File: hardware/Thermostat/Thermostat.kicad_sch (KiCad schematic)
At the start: 46 parts, among them J1 Barrel_Jack_Switch, J2 Conn_01x02_Pin, J3 AVR-ISP-6, J4 MainConnectorr, K1 G6E, K2 G6E, K3 G6E, K4 G6E, SW1 12MM, SW2 12MM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

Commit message: Battery?
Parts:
- added BT1: Battery_Cell, Battery:BatteryHolder_LINX_BAT-HLD-012-SMT, symbol Device:Battery_Cell
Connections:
- net GND: now also BT1.2 (-); no longer U8.3 (VBAT)
- new net: BT1.1 (+), U8.3 (VBAT)
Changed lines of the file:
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@@
+	)
+	(symbol
+		(lib_id "Device:Battery_Cell")
+		(at 182.88 137.16 90)
+		(unit 1)
+		(exclude_from_sim no)
+		(in_bom yes)
+		(on_board yes)
+		(dnp no)
+		(property "Reference" "BT1"
+			(at 193.802 136.652 90)
+			(effects
+				(font
+					(size 1.27 1.27)
+				)
+			)
+		)
+		(property "Value" "Battery_Cell"
+			(at 188.214 134.62 90)
+			(effects
+				(font
+					(size 1.27 1.27)
+				)
+			)
+		)
+		(property "Footprint" "Battery:BatteryHolder_LINX_BAT-HLD-012-SMT"
+			(at 181.356 137.16 90)
+			(effects
+				(font
+					(size 1.27 1.27)
+				)
+				(hide yes)
+			)
+		)
+		(property "Datasheet" "~"
+			(at 181.356 137.16 90)
+			(effects
+				(font
+					(size 1.27 1.27)
+				)
+				(hide yes)
+			)
+		)
+		(property "Description" "Single-cell battery"
+			(at 182.88 137.16 0)
+			(effects
+				(font
+					(size 1.27 1.27)
+				)
+				(hide yes)
+			)
+		)
+		(property "Sim.Device" "V"
+			(at 182.88 137.16 0)
+			(effects
+				(font
+					(size 1.27 1.27)
+				)
+				(hide yes)
+			)
+		)
+		(property "Sim.Type" "DC"
+			(at 182.88 137.16 0)
+			(effects
+				(font
+					(size 1.27 1.27)
+				)
+				(hide yes)
+			)
+		)
+		(property "Sim.Pins" "1=+ 2=-"
+			(at 182.88 137.16 0)
+			(effects
+				(font
+					(size 1.27 1.27)
+				)
+				(hide yes)
+			)
+		)
+		(pin "2"
+		)
+		(pin "1"
+		)
+		(instances
+			(project ""
+				(path "/dae3c193-ffe6-4911-a810-cfe956c95f3b"
+					(reference "BT1")
+					(unit 1)
+				)
+			)
+		)
 	)
 	(symbol
@@
 	(symbol
 		(lib_id "power:GND")
-		(at 177.8 137.16 90)
+		(at 185.42 137.16 90)
 		(unit 1)
 		(exclude_from_sim no)
@@
 		(dnp no)
 		(property "Reference" "#PWR030"
-			(at 184.15 137.16 0)
+			(at 191.77 137.16 0)
 			(effects
 				(font
@@
 		)
 		(property "Value" "GND"
-			(at 182.372 137.16 90)
+			(at 189.992 137.16 90)
 			(effects
 				(font
@@
 		)
 		(property "Footprint" ""
-			(at 177.8 137.16 0)
+			(at 185.42 137.16 0)
 			(effects
 				(font
@@
 		)
 		(property "Datasheet" ""
-			(at 177.8 137.16 0)
+			(at 185.42 137.16 0)
 			(effects
 				(font
@@
 		)
 		(property "Description" "Power symbol creates a global label with name \"GND\" , ground"
-			(at 177.8 137.16 0)
-			(effects
-				(font
+			(at 185.42 137.16 0)
+			(effects
+				(font

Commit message: Get in battery
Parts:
- BT1: footprint Battery:BatteryHolder_LINX_BAT-HLD-012-SMT -> Battery:BatteryHolder_Keystone_3000_1x12mm
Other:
- moved on the sheet: BT1, C10, C7, C8, C9, R6, R7, U1, U2, U8, U9, Y3

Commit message: Fixes from Cyber City Circuits review
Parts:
- removed D5: 1N4007, Diode_THT:D_DO-41_SOD81_P10.16mm_Horizontal, symbol Diode:1N4007
- added D1: SS33, Diode_SMD:D_SMA, symbol Diode:SS33
- added R2: 4.7k, Resistor_SMD:R_0603_1608Metric, symbol Device:R_US
- R1: value 5k -> 10k
- R6, R7: value 5k -> 4.7k
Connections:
- net +5V: now also U5.18 (AVCC), U5.20 (AREF), R2.1; no longer U1.6 (^RESET)
- net 24VDC: now also D1.1 (K)
- net GND: no longer U5.18 (AVCC), U5.20 (AREF)
- net at J1.1: now also D1.2 (A)
- net ^SCRESET: now reaches U5.12 (PB0)
- net ^SCRESET: now also U1.6 (^RESET), R2.2
- no-connect marks 16 -> 15

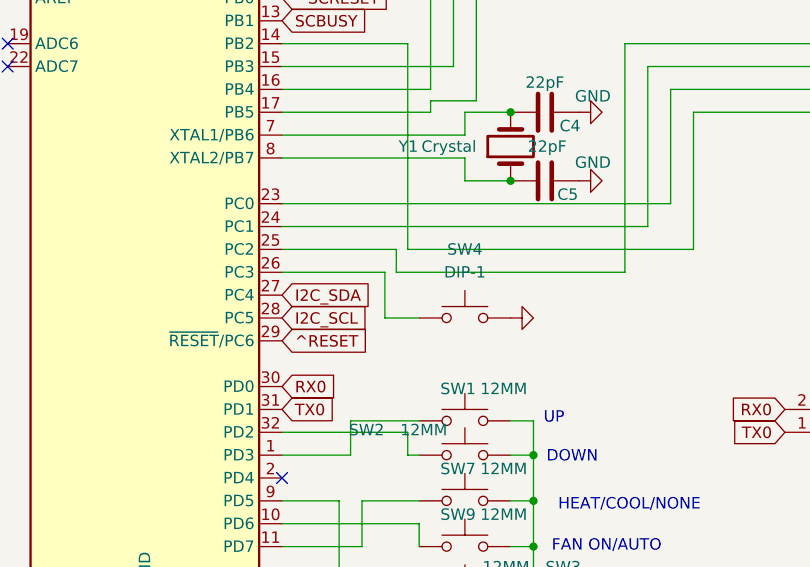
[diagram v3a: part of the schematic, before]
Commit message: Remove physical Reverse Valve button and put it in save state instead
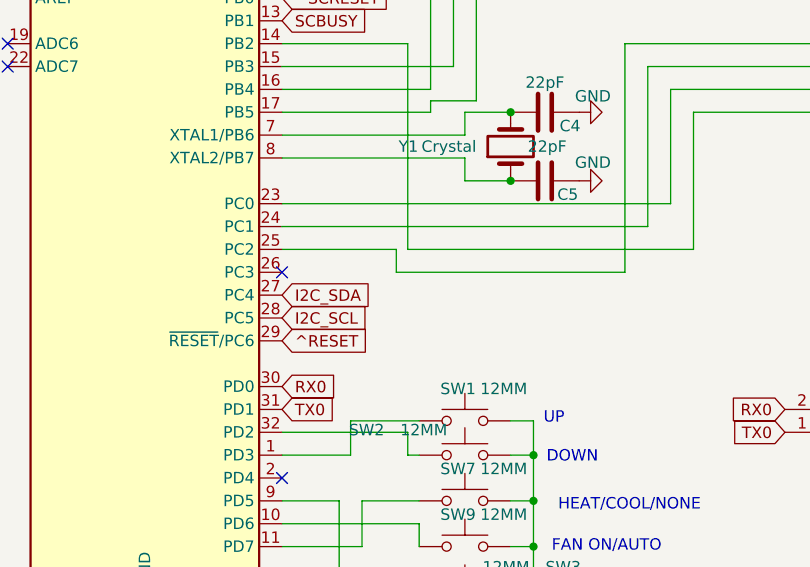
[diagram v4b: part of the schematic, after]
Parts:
- removed SW4: DIP-1, Button_Switch_SMD:SW_DIP_SPSTx01_Slide_6.7x4.1mm_W6.73mm_P2.54mm_LowProfile_JPin, symbol Switch:SW_Push
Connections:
- no-connect marks 15 -> 16
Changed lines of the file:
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@@
 	)
 	(no_connect
+		(at 50.8 140.97)
+	)
+	(no_connect
 		(at 113.03 87.63)
 	)
@@
 	(wire
 		(pts
-			(xy 62.23 140.97) (xy 62.23 146.05)
-		)
-		(stroke
-			(width 0)
-			(type default)
-		)
-	)
-	(wire
-		(pts
 			(xy 137.16 39.37) (xy 137.16 40.64)
 		)
@@
 	(wire
 		(pts
-			(xy 62.23 146.05) (xy 66.04 146.05)
-		)
-		(stroke
-			(width 0)
-			(type default)
-		)
-	)
-	(wire
-		(pts
 			(xy 119.38 110.49) (xy 121.92 110.49)
 		)
@@
 	(wire
 		(pts
-			(xy 50.8 140.97) (xy 62.23 140.97)
-		)
-		(stroke
-			(width 0)
-			(type default)
-		)
-	)
-	(wire
-		(pts
 			(xy 152.4 38.1) (xy 152.4 40.64)
 		)
@@
 	)
 	(symbol
-		(lib_id "Switch:SW_Push")
-		(at 71.12 146.05 0)
-		(unit 1)
-		(exclude_from_sim no)
-		(in_bom yes)
-		(on_board yes)
-		(dnp no)
-		(fields_autoplaced yes)
-		(property "Reference" "SW4"
-			(at 71.12 138.43 0)
-			(effects
-				(font
-					(size 1.27 1.27)
-				)
-			)
-		)
-		(property "Value" "DIP-1"
-			(at 71.12 140.97 0)
-			(effects
-				(font
-					(size 1.27 1.27)
-				)
-			)
-		)
-		(property "Footprint" "Button_Switch_SMD:SW_DIP_SPSTx01_Slide_6.7x4.1mm_W6.73mm_P2.54mm_LowProfile_JPin"
-			(at 71.12 140.97 0)
-			(effects
-				(font
-					(size 1.27 1.27)
-				)
-				(hide yes)
-			)
-		)
-		(property "Datasheet" "~"
-			(at 71.12 140.97 0)
-			(effects
-				(font
-					(size 1.27 1.27)
-				)
-				(hide yes)
-			)
-		)
-		(property "Description" "Push button switch, generic, two pins"
-			(at 71.12 146.05 0)
-			(effects
-				(font
-					(size 1.27 1.27)
-				)
-				(hide yes)
-			)
-		)
-		(pin "2"
-		)
-		(pin "1"
-		)
-		(instances
-			(project "Thermostat"
-				(path "/dae3c193-ffe6-4911-a810-cfe956c95f3b"
-					(reference "SW4")
-					(unit 1)
-				)
-			)
-		)
-	)
-	(symbol
 		(lib_id "power:+5V")
 		(at 207.01 123.19 0)
@@
 					(unit 1)
 				)
-			)
-		)
-	)
-	(symbol
-		(lib_id "power:GND")
-		(at 76.2 146.05 90)
-		(unit 1)
-		(exclude_from_sim no)
-		(in_bom yes)
-		(on_board yes)
-		(dnp no)
-		(property "Reference" "#PWR06"
-			(at 82.55 146.05 0)
-			(effects
-				(font
-					(size 1.27 1.27)
-				)
-				(hide yes)
-			)
-		)
-		(property "Value" "GND"
-			(at 83.058 147.828 90)
-			(effects
-				(font
-					(size 1.27 1.27)
-				)
-				(hide yes)
-			)
-		)
-		(property "Footprint" ""
-			(at 76.2 146.05 0)
-			(effects
-				(font
-					(size 1.27 1.27)
-				)
-				(hide yes)
-			)
-		)
-		(property "Datasheet" ""
-			(at 76.2 146.05 0)
-			(effects
-				(font
-					(size 1.27 1.27)
-				)
-				(hide yes)
-			)
-		)
-		(property "Description" "Power symbol creates a global label with name \"GND\" , ground"
-			(at 76.2 146.05 0)
-			(effects
-				(font
-					(size 1.27 1.27)
-				)
-				(hide yes)
-			)
-		)
-		(pin "1"
-		)
-		(instances
-			(project "Thermostat"
-				(path "/dae3c193-ffe6-4911-a810-cfe956c95f3b"
-					(reference "#PWR06")
-					(unit 1)
-				)

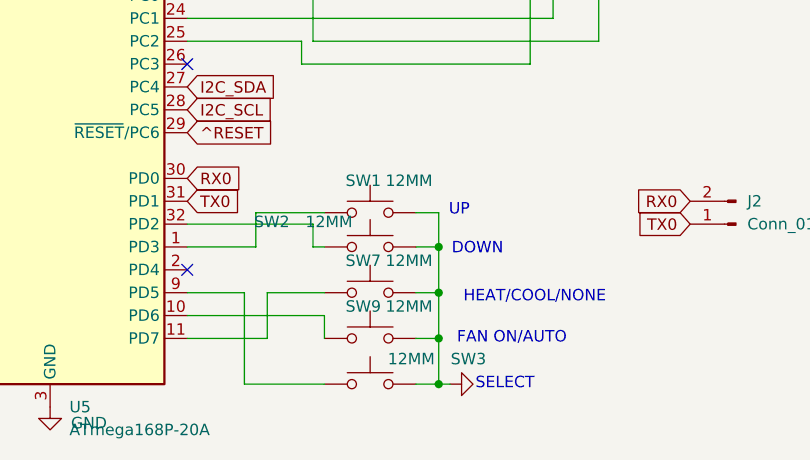
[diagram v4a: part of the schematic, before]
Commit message: Put switches in order and move resistor
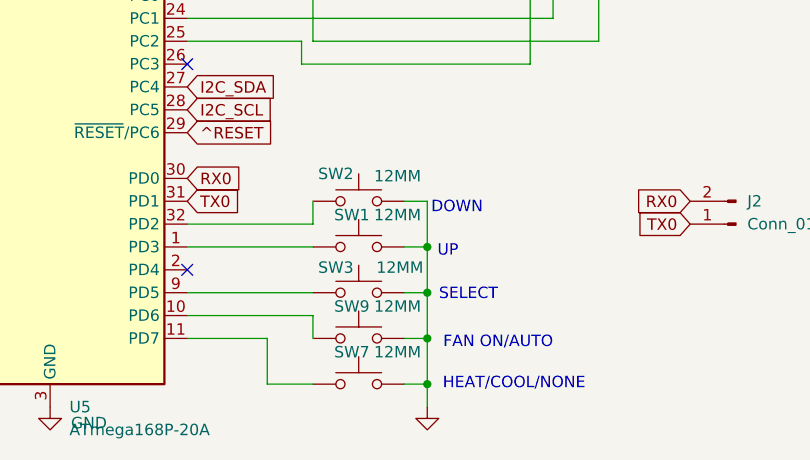
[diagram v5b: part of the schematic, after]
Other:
- moved on the sheet: SW1, SW2, SW3, SW7, SW9

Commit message: Hardware work
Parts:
- removed J1: Barrel_Jack_Switch, Connector_BarrelJack:BarrelJack_Wuerth_6941xx301002, symbol Connector:Barrel_Jack_Switch
- added J5: Screw_Terminal_01x02, TerminalBlock_MetzConnect:TerminalBlock_MetzConnect_Type094_RT03502HBLU_1x02_P5.00mm_Horizontal, symbol Connector:Screw_Terminal_01x02
- BT1: footprint Battery:BatteryHolder_Keystone_3000_1x12mm -> ThermostatFootprints:BS-12-B3AA011
- C1, C2, C3: footprint Capacitor_SMD:C_1808_4520Metric -> Capacitor_SMD:C_1210_3225Metric
- U3: value ~ -> (none)
- Y3: footprint Crystal:Crystal_SMD_5032-2Pin_5.0x3.2mm -> Crystal:Crystal_SMD_3215-2Pin_3.2x1.5mm
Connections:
- net GND: now also J5.1 (Pin_1)
- net at D1.2 (A): now also J5.2 (Pin_2)

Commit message: Good more hardware work
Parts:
- J3: footprint Connector_PinHeader_2.54mm:PinHeader_2x03_P2.54mm_Vertical_SMD -> ThermostatFootprints:PinHeader_2x03_P2.54mm_Vertical_SMD_2
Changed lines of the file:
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@@
 			)
 		)
-		(property "Footprint" "Connector_PinHeader_2.54mm:PinHeader_2x03_P2.54mm_Vertical_SMD"
+		(property "Footprint" "ThermostatFootprints:PinHeader_2x03_P2.54mm_Vertical_SMD_2"
 			(at 71.12 83.82 90)
 			(hide yes)
